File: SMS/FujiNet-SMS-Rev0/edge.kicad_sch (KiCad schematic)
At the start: 3 parts, among them J1 SMS_Cart_Edge_50

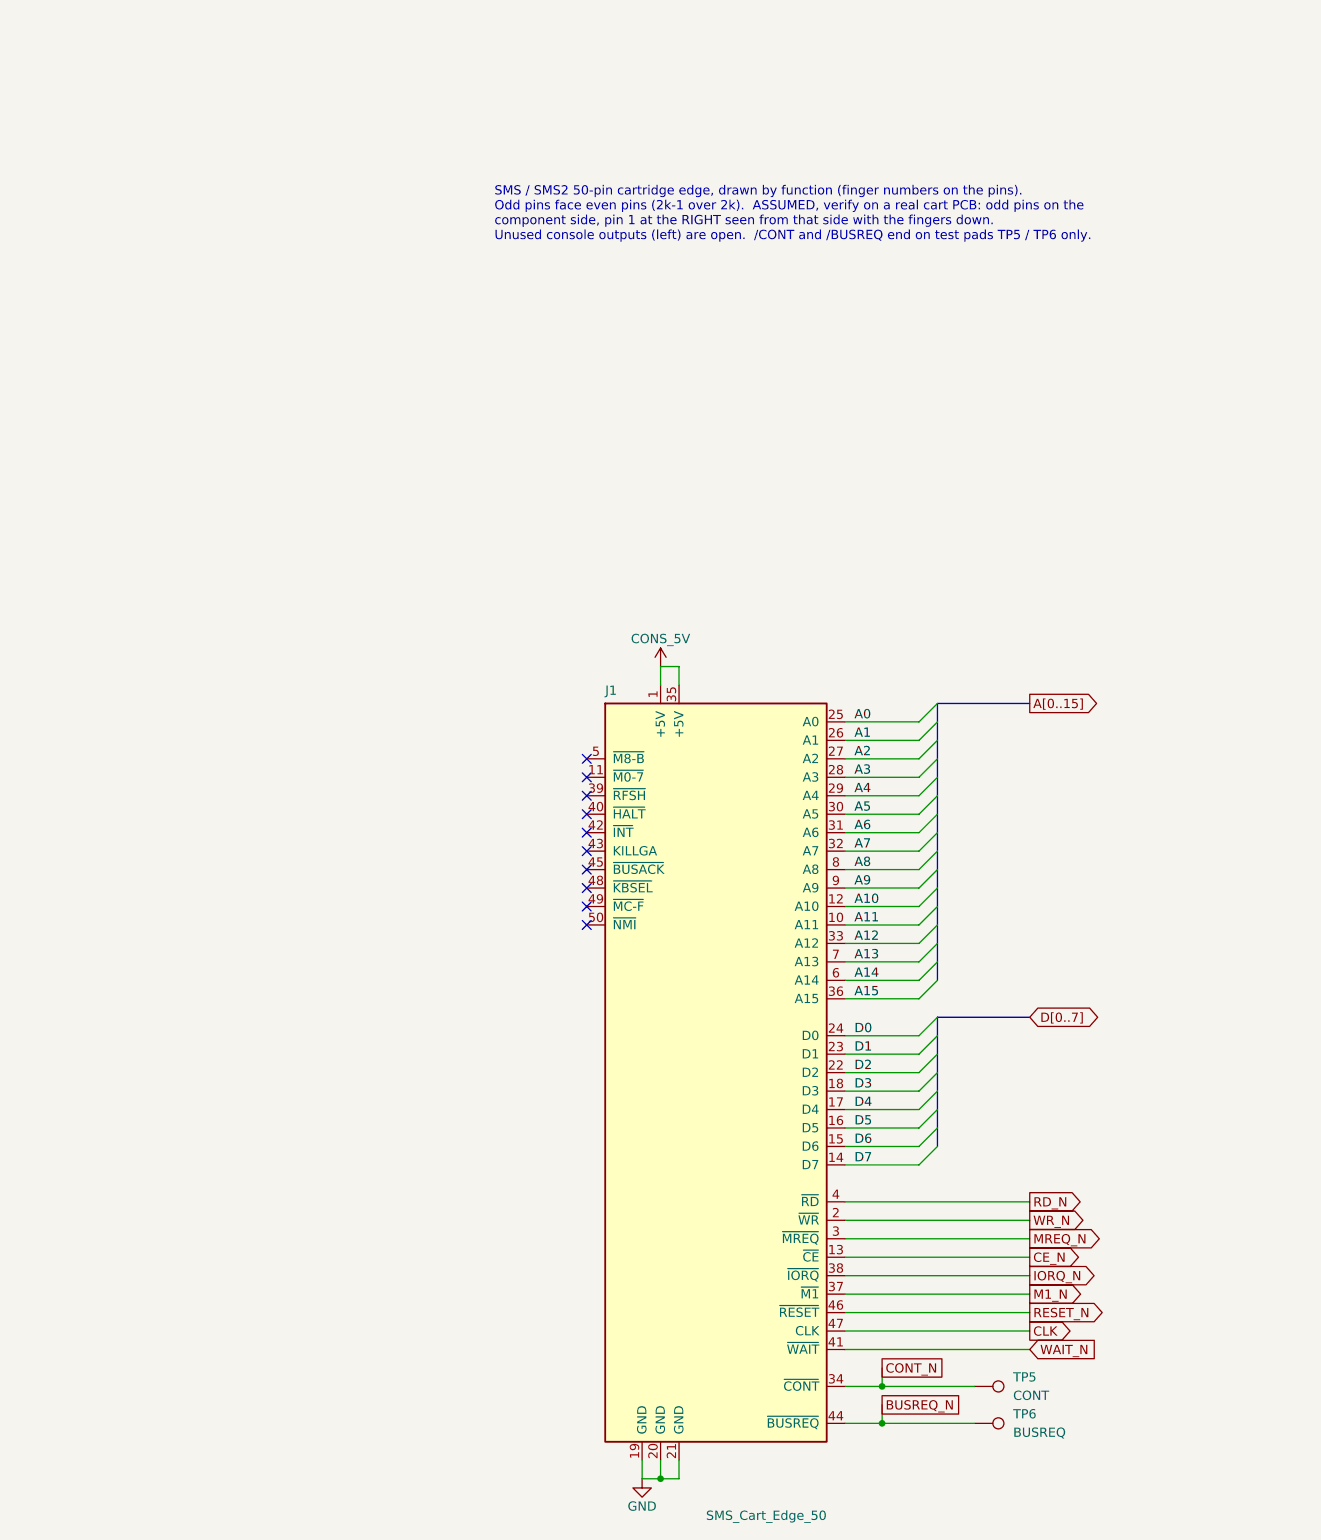
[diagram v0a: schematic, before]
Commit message: SMS Rev0: audit with kicad-happy + datasheets, fix the edge, redraw the schematic
Edge connector: every source (SMS Power slot diagram, little-scale, a 171-5519
scan, raphnet, the barbeque and reidrac footprints) puts the EVEN pins on the
component / label side with pins 1/2 at the right.  The schematic-only
footprint had the faces swapped, which would have put console +5V on /WR.
make_edge_fp.py now writes even pads on F.Cu, odd on B.Cu, 1.75 x 8.75 mm
fingers 0.75-9.5 mm from the edge on a 65.8 mm tab; check_nets.py asserts it
and tools/audit/edge_orientation.py checks it against the sources.

kicad-happy + datasheet audit (docs/design-review-rev0.md Part 1, 27 deep
review findings, gate 27/27): R_VBPD 4.7k VBUS pull-down (SS34 leakage lifts
the P-FET gate), /WAIT gate pull-up 10k -> 4.7k (GPIO34's reset pull-down vs
the 2N7002's 2.5 V threshold), 10 uF bulk on the console 5V.

Schematic: hierarchical sheets wired on a root block diagram (edge -> RP2354B
-> ESP32-S3 -> USB, glue and SRAM under the RP, power below); every sheet
drawn left to right, the glue as a wired logic network by gate depth, the
RP2354B mirrored so its bus faces the console, small sheets on A4.  Parts
are addressed by key (design.py), no more NES reference aliasing.  sch_draw
gains hierarchical labels, sheet blocks, a bus graph and flag / power-pin
lints; gen_sch checks the hierarchy against design.py and names nets by
their last path element (one bus vector per bus: KiCad joins differing
vectors by position).  ERC 0, check_nets 437/437, check_glue 8192/8192.

JLC CPL rotations measured against the EasyEDA footprint of every LCSC part
(tools/audit/jlc); the AS6C4008 has no EasyEDA footprint.

Co-Authored-By: Claude Opus 5.5 <noreply@anthropic.com>
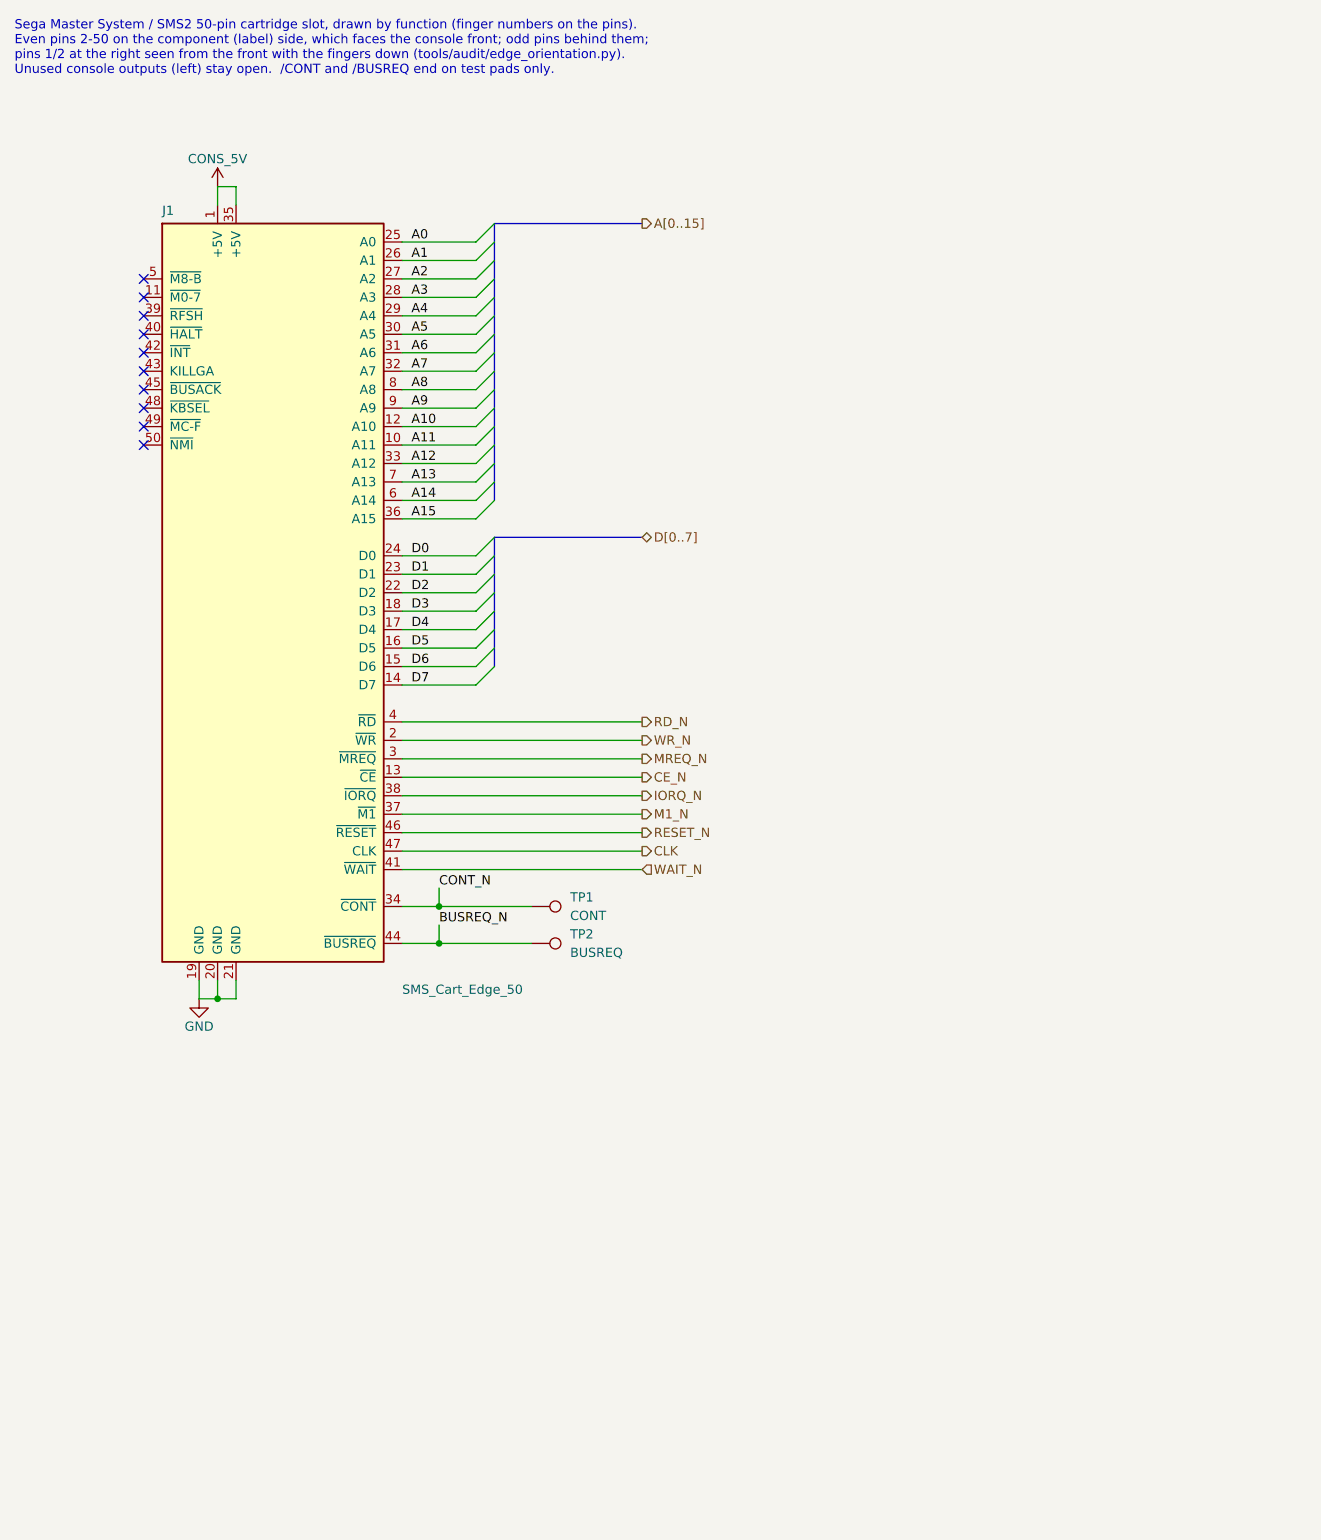
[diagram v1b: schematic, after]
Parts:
- removed TP5: CONT, FujiNet-SMS:TestPoint_Pad_D1.5mm, symbol Connector:TestPoint
- removed TP6: BUSREQ, FujiNet-SMS:TestPoint_Pad_D1.5mm, symbol Connector:TestPoint
- added TP1: CONT, FujiNet-SMS:TestPoint_Pad_D1.5mm, symbol Connector:TestPoint
- added TP2: BUSREQ, FujiNet-SMS:TestPoint_Pad_D1.5mm, symbol Connector:TestPoint
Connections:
- net BUSREQ_N: now also TP2.1
- net CONT_N: now also TP1.1
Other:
- note added: "Sega Master System / SMS2 50-pin cartridge slot, drawn by function (finger numbers on the pins). Even pins 2-50 on the component (label) side, which faces the console front; odd pins behind them; pins 1/2 at the right seen from the front with the fingers down (tools/audit/edge_orientation.py). Unused console outputs (left) stay open. /CONT and /BUSREQ end on test pads only."
- note removed: "SMS / SMS2 50-pin cartridge edge, drawn by function (finger numbers on the pins). Odd pins face even pins (2k-1 over 2k). ASSUMED, verify on a real cart PCB: odd pins on the component side, pin 1 at the RIGHT seen from that side with the fingers down. Unused console outputs (left) are open. /CONT and /BUSREQ end on test pads TP5 / TP6 only."
- moved on the sheet: J1
